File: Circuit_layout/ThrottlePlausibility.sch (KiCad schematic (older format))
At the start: 56 parts, among them Q2 MMBF170, SW1 TS5A3159-Q1, U1 LM7332, U17 MCP6004, U3 MCP6004, U4 MCP6004, U5 LM7332, U6 LM339, U8 74ACT11030

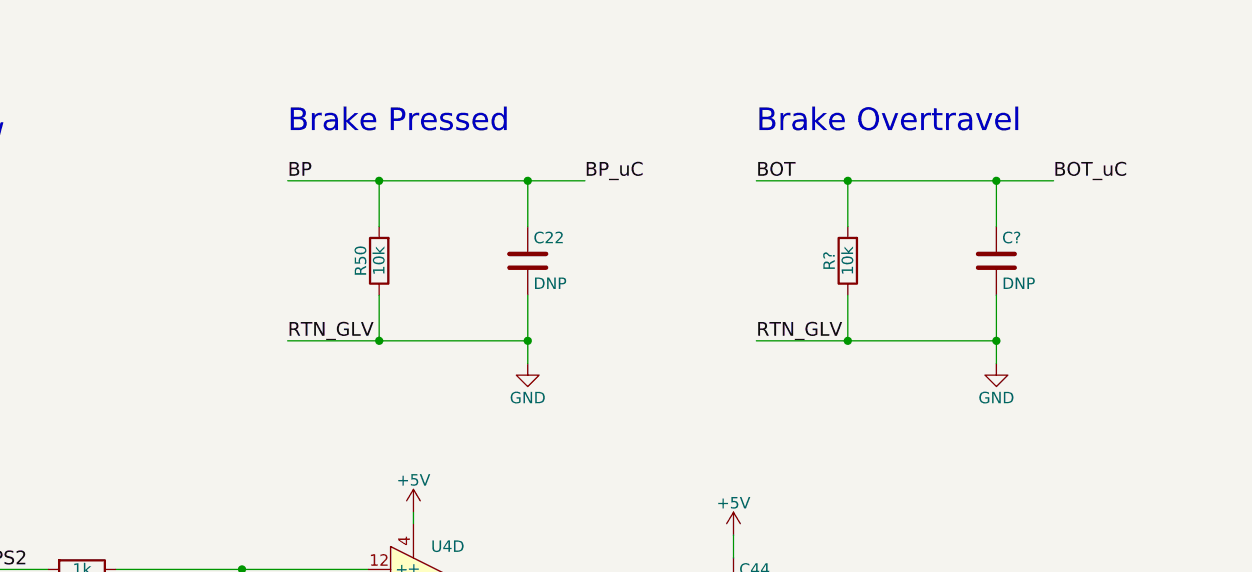
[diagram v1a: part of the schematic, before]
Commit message: added optoiso for brake overtravel
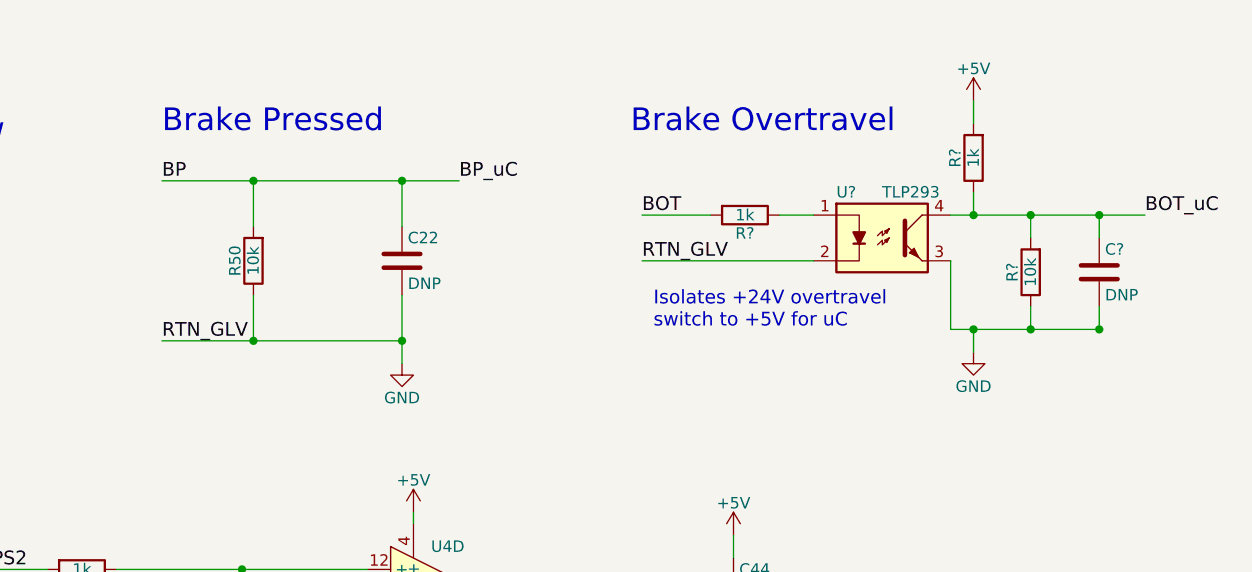
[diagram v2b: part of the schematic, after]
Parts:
- removed C?: DNP, Capacitors_SMD:C_0805_HandSoldering, symbol C
- removed R?: 10k, Resistors_SMD:R_0805_HandSoldering, symbol R
- added C?: DNP, Capacitors_SMD:C_0805_HandSoldering, symbol C
- added R? (x2): 1k, Resistors_SMD:R_0805_HandSoldering, symbol R
- added R?: 10k, Resistors_SMD:R_0805_HandSoldering, symbol R
- added U?: TLP293, Housings_SSOP:SOP-4_4.4x2.8mm_Pitch1.27mm, symbol TLP291
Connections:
- wire segments 182 -> 189
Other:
- note added: "Isolates +24V overtravel \nswitch to +5V for uC"
- moved on the sheet: C22, R50
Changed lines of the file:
@@
 BP_uC
 Wire Wire Line
-	12350 2150 12350 1950
-Text Label 11950 1450 0    60   ~ 0
+	11800 2150 11800 1950
+Text Label 11400 1450 0    60   ~ 0
 BP
 Wire Wire Line
-	12350 1450 12350 1650
-Text Label 11950 2150 0    60   ~ 0
+	11800 1450 11800 1650
+Text Label 11400 2150 0    60   ~ 0
 RTN_GLV
 Wire Wire Line
-	11950 1450 13250 1450
-Wire Wire Line
-	11950 2150 13000 2150
-Connection ~ 12350 1450
-Connection ~ 12350 2150
+	11400 1450 12700 1450
+Wire Wire Line
+	11400 2150 12450 2150
+Connection ~ 11800 1450
+Connection ~ 11800 2150
 $Comp
 L C C22
 U 1 1 58AE29E7
-P 13000 1800
-F 0 "C22" H 13025 1900 50  0000 L CNN
-F 1 "DNP" H 13025 1700 50  0000 L CNN
-F 2 "Capacitors_SMD:C_0805_HandSoldering" H 13038 1650 50  0001 C CNN
-F 3 "" H 13000 1800 50  0000 C CNN
-	1    13000 1800
-	1    0    0    -1
-$EndComp
-Wire Wire Line
-	13000 1950 13000 2250
-Connection ~ 13000 2150
-Wire Wire Line
-	13000 1650 13000 1450
-Connection ~ 13000 1450
-Text Label 13250 1450 0    60   ~ 0
+P 12450 1800
+F 0 "C22" H 12475 1900 50  0000 L CNN
+F 1 "DNP" H 12475 1700 50  0000 L CNN
+F 2 "Capacitors_SMD:C_0805_HandSoldering" H 12488 1650 50  0001 C CNN
+F 3 "" H 12450 1800 50  0000 C CNN
+	1    12450 1800
+	1    0    0    -1
+$EndComp
+Wire Wire Line
+	12450 1950 12450 2250
+Connection ~ 12450 2150
+Wire Wire Line
+	12450 1650 12450 1450
+Connection ~ 12450 1450
+Text Label 12700 1450 0    60   ~ 0
 BP_uC
 Wire Wire Line
@@
 Text Label 3600 1100 0    60   ~ 0
 RTN_GLV
-Text Notes 11950 1250 0    99   ~ 0
+Text Notes 11400 1250 0    99   ~ 0
 Brake Pressed
 $Comp
 L GND #PWR087
 U 1 1 58B4B2A9
-P 13000 2250
-F 0 "#PWR087" H 13000 2000 50  0001 C CNN
-F 1 "GND" H 13000 2100 50  0000 C CNN
-F 2 "" H 13000 2250 50  0000 C CNN
-F 3 "" H 13000 2250 50  0000 C CNN
-	1    13000 2250
+P 12450 2250
+F 0 "#PWR087" H 12450 2000 50  0001 C CNN
+F 1 "GND" H 12450 2100 50  0000 C CNN
+F 2 "" H 12450 2250 50  0000 C CNN
+F 3 "" H 12450 2250 50  0000 C CNN
+	1    12450 2250
 	1    0    0    -1
 $EndComp
@@
 L R R50
 U 1 1 58B79345
-P 12350 1800
-F 0 "R50" V 12430 1800 50  0000 C CNN
-F 1 "10k" V 12350 1800 50  0000 C CNN
-F 2 "Resistors_SMD:R_0805_HandSoldering" V 12280 1800 50  0001 C CNN
-F 3 "" H 12350 1800 50  0000 C CNN
-F 4 "P10.0KCCT-ND" V 12350 1800 60  0001 C CNN "DigiKey P/N"
-F 5 "http://www.digikey.com/product-detail/en/panasonic-electronic-components/ERJ-6ENF1002V/P10.0KCCT-ND/119248" V 12350 1800 60  0001 C CNN "URL"
-F 6 "ERJ-6ENF1002V" V 12350 1800 60  0001 C CNN "Man P/N"
-	1    12350 1800
+P 11800 1800
+F 0 "R50" V 11880 1800 50  0000 C CNN
+F 1 "10k" V 11800 1800 50  0000 C CNN
+F 2 "Resistors_SMD:R_0805_HandSoldering" V 11730 1800 50  0001 C CNN
+F 3 "" H 11800 1800 50  0000 C CNN
+F 4 "P10.0KCCT-ND" V 11800 1800 60  0001 C CNN "DigiKey P/N"
+F 5 "http://www.digikey.com/product-detail/en/panasonic-electronic-components/ERJ-6ENF1002V/P10.0KCCT-ND/119248" V 11800 1800 60  0001 C CNN "URL"
+F 6 "ERJ-6ENF1002V" V 11800 1800 60  0001 C CNN "Man P/N"
+	1    11800 1800
 	-1   0    0    1
 $EndComp
@@
 $EndComp
 Connection ~ 3100 6000
-Wire Wire Line
-	14400 2150 14400 1950
-Text Label 14000 1450 0    60   ~ 0
-BOT
-Wire Wire Line
-	14400 1450 14400 1650
-Text Label 14000 2150 0    60   ~ 0
+Text Label 13500 1800 0    60   ~ 0
 RTN_GLV
-Wire Wire Line
-	14000 1450 15300 1450
-Wire Wire Line
-	14000 2150 15050 2150
-Connection ~ 14400 1450
-Connection ~ 14400 2150
-$Comp
-L C C?
-U 1 1 58BE3051
-P 15050 1800
-F 0 "C?" H 15075 1900 50  0000 L CNN
-F 1 "DNP" H 15075 1700 50  0000 L CNN
-F 2 "Capacitors_SMD:C_0805_HandSoldering" H 15088 1650 50  0001 C CNN
-F 3 "" H 15050 1800 50  0000 C CNN
-	1    15050 1800
-	1    0    0    -1
-$EndComp
-Wire Wire Line
-	15050 1950 15050 2250
-Connection ~ 15050 2150
-Wire Wire Line
-	15050 1650 15050 1450
-Connection ~ 15050 1450
-Text Label 15300 1450 0    60   ~ 0
-BOT_uC
-Text Notes 14000 1250 0    99   ~ 0
+Text Notes 13450 1250 0    99   ~ 0
 Brake Overtravel
-$Comp
-L GND #PWR?
-U 1 1 58BE305D
-P 15050 2250
-F 0 "#PWR?" H 15050 2000 50  0001 C CNN
-F 1 "GND" H 15050 2100 50  0000 C CNN
-F 2 "" H 15050 2250 50  0000 C CNN
-F 3 "" H 15050 2250 50  0000 C CNN
-	1    15050 2250
-	1    0    0    -1
-$EndComp
-$Comp
-L R R?
-U 1 1 58BE3067
-P 14400 1800
-F 0 "R?" V 14480 1800 50  0000 C CNN
-F 1 "10k" V 14400 1800 50  0000 C CNN
-F 2 "Resistors_SMD:R_0805_HandSoldering" V 14330 1800 50  0001 C CNN
-F 3 "" H 14400 1800 50  0000 C CNN
-F 4 "P10.0KCCT-ND" V 14400 1800 60  0001 C CNN "DigiKey P/N"
-F 5 "http://www.digikey.com/product-detail/en/panasonic-electronic-components/ERJ-6ENF1002V/P10.0KCCT-ND/119248" V 14400 1800 60  0001 C CNN "URL"
-F 6 "ERJ-6ENF1002V" V 14400 1800 60  0001 C CNN "Man P/N"
-	1    14400 1800
-	-1   0    0    1
-$EndComp
 Wire Wire Line
 	3250 1500 3450 1500
@@
 Text Label 3400 1950 0    60   ~ 0
 BOT_uC
+$Comp
+L TLP291 U?
+U 1 1 58BF52E8
+P 14550 1700
+F 0 "U?" H 14350 1900 50  0000 L CNN
+F 1 "TLP293" H 14550 1900 50  0000 L CNN
+F 2 "Housings_SSOP:SOP-4_4.4x2.8mm_Pitch1.27mm" H 14350 1500 50  0001 L CIN
+F 3 "" H 14550 1700 50  0000 L CNN
+F 4 "TLP293(GB-TPLECT-ND" H 14550 1700 60  0001 C CNN "DigiKey P/N"
+F 5 "http://www.digikey.com/product-detail/en/toshiba-semiconductor-and-storage/TLP293(GB-TPL,E/TLP293(GB-TPLECT-ND/4562965" H 14550 1700 60  0001 C CNN "URL"
+F 6 "TLP293(GB-TPLE" H 14550 1700 60  0001 C CNN "Man P/N"
+F 7 "http://www.digikey.com/product-detail/en/toshiba-semiconductor-and-storage/TLP291(GB-TP,SE/TLP291(GB-TPSECT-ND/4562949" H 14550 1700 60  0001 C CNN "TLP291"
+	1    14550 1700
+	1    0    0    -1
+$EndComp
+$Comp
+L R R?
+U 1 1 58BF52F2
+P 13950 1600
+F 0 "R?" V 14030 1600 50  0000 C CNN
+F 1 "1k" V 13950 1600 50  0000 C CNN
+F 2 "Resistors_SMD:R_0805_HandSoldering" V 13880 1600 50  0001 C CNN
+F 3 "" H 13950 1600 50  0000 C CNN
+F 4 "P1.00KCCT-ND" V 13950 1600 60  0001 C CNN "DigiKey P/N"
+F 5 "http://www.digikey.com/product-detail/en/panasonic-electronic-components/ERJ-6ENF1001V/P1.00KCCT-ND/118957" V 13950 1600 60  0001 C CNN "URL"
+F 6 "ERJ-6ENF1001V" V 13950 1600 60  0001 C CNN "Man P/N"
+	1    13950 1600
+	0    1    1    0
+$EndComp
+$Comp
+L R R?
+U 1 1 58BF52FC
+P 14950 1350
+F 0 "R?" V 15030 1350 50  0000 C CNN
+F 1 "1k" V 14950 1350 50  0000 C CNN
+F 2 "Resistors_SMD:R_0805_HandSoldering" V 14880 1350 50  0001 C CNN
+F 3 "" H 14950 1350 50  0000 C CNN
+F 4 "P1.00KCCT-ND" V 14950 1350 60  0001 C CNN "DigiKey P/N"
+F 5 "http://www.digikey.com/product-detail/en/panasonic-electronic-components/ERJ-6ENF1001V/P1.00KCCT-ND/118957" V 14950 1350 60  0001 C CNN "URL"
+F 6 "ERJ-6ENF1001V" V 14950 1350 60  0001 C CNN "Man P/N"
+	1    14950 1350
+	-1   0    0    1
+$EndComp
+$Comp
+L GND #PWR?
+U 1 1 58BF5303
+P 14950 2200
+F 0 "#PWR?" H 14950 1950 50  0001 C CNN
+F 1 "GND" H 14950 2050 50  0000 C CNN
+F 2 "" H 14950 2200 50  0000 C CNN
+F 3 "" H 14950 2200 50  0000 C CNN
+	1    14950 2200
+	1    0    0    -1
+$EndComp
+$Comp
+L +5V #PWR?
+U 1 1 58BF60CD
+P 14950 1100
+F 0 "#PWR?" H 14950 950 50  0001 C CNN
+F 1 "+5V" H 14950 1240 50  0000 C CNN
+F 2 "" H 14950 1100 50  0000 C CNN
+F 3 "" H 14950 1100 50  0000 C CNN
+	1    14950 1100
+	1    0    0    -1
+$EndComp
+$Comp
+L R R?
+U 1 1 58BF69A9
+P 15200 1850
+F 0 "R?" V 15280 1850 50  0000 C CNN
+F 1 "10k" V 15200 1850 50  0000 C CNN
+F 2 "Resistors_SMD:R_0805_HandSoldering" V 15130 1850 50  0001 C CNN
+F 3 "" H 15200 1850 50  0000 C CNN
+F 4 "P10.0KCCT-ND" V 15200 1850 60  0001 C CNN "DigiKey P/N"
+F 5 "http://www.digikey.com/product-detail/en/panasonic-electronic-components/ERJ-6ENF1002V/P10.0KCCT-ND/119248" V 15200 1850 60  0001 C CNN "URL"
+F 6 "ERJ-6ENF1002V" V 15200 1850 60  0001 C CNN "Man P/N"
+	1    15200 1850
+	-1   0    0    1
+$EndComp
+$Comp
+L C C?
+U 1 1 58BF6C5C
+P 15500 1850
+F 0 "C?" H 15525 1950 50  0000 L CNN
+F 1 "DNP" H 15525 1750 50  0000 L CNN
+F 2 "Capacitors_SMD:C_0805_HandSoldering" H 15538 1700 50  0001 C CNN
+F 3 "" H 15500 1850 50  0000 C CNN
+	1    15500 1850
+	1    0    0    -1
+$EndComp
+Wire Wire Line
+	15500 1600 15500 1700
+Connection ~ 15500 1600
+Text Label 15700 1600 0    60   ~ 0
+BOT_uC
+Wire Wire Line
+	14850 1800 14850 2100
+Wire Wire Line
+	15500 2100 15500 2000
+Connection ~ 15500 2100
+Text Label 13500 1600 0    60   ~ 0
+BOT
+Wire Wire Line
+	13500 1600 13800 1600
+Wire Wire Line
+	14100 1600 14250 1600
+Wire Wire Line
+	13500 1800 14250 1800
+Wire Wire Line
+	14850 1600 15700 1600
+Wire Wire Line
+	14950 1500 14950 1600
+Connection ~ 14950 1600
+Wire Wire Line
+	15200 1700 15200 1600
+Connection ~ 15200 1600
+Wire Wire Line
+	14850 2100 15500 2100
+Wire Wire Line
+	15200 2100 15200 2000
+Connection ~ 15200 2100
+Wire Wire Line
+	14950 2200 14950 2100
+Connection ~ 14950 2100
+Wire Wire Line
+	14950 1100 14950 1200
+Text Notes 13550 2100 0    60   ~ 0
+Isolates +24V overtravel \nswitch to +5V for uC
 $EndSCHEMATC

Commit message: need to make further changes after review w/ prof
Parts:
- removed C20, C24: 15p, Capacitors_SMD:C_0805_HandSoldering, symbol C
- removed R?: 1k, Resistors_SMD:R_0805_HandSoldering, symbol R
- removed SW1: TS5A3159-Q1, TO_SOT_Packages_SMD:SOT-23-6_Handsoldering, symbol TS5A3159-Q1
- added JP?: JUMPER3, symbol JUMPER3
- added R?: 10k, Resistors_SMD:R_0805_HandSoldering, symbol R
- added U? (x2): MCP6004, Housings_SOIC:SOIC-14_3.9x8.7mm_Pitch1.27mm, symbol MCP6004
- renumbered U17 to U3
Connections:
- wire segments 189 -> 188
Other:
- note added: "Add brake input"
- note added: "Change to jumper"
- note added: "Fix BOT"
- note added: "Inv. signal\nCurr. Xfer. Ratio=200% \n(w/in rng)"
- note removed: "Isolates +24V overtravel \nswitch to +5V for uC"
- moved on the sheet: R25

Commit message: changes before presentation
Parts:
- removed C13, C39: 0.1u, Capacitors_SMD:C_0805_HandSoldering, symbol C
- removed C?: DNP, Capacitors_SMD:C_0805_HandSoldering, symbol C
- removed R21, R?: 1k, Resistors_SMD:R_0805_HandSoldering, symbol R
- removed R? (x2): 10k, Resistors_SMD:R_0805_HandSoldering, symbol R
- removed U1, U5: LM7332, Housings_SOIC:SOIC-8_3.9x4.9mm_Pitch1.27mm, symbol LM7332
- removed U6: LM339, Housings_SOIC:SOIC-14_3.9x8.7mm_Pitch1.27mm, symbol LM339
- removed U?: BAJ0CC0FP-E2, symbol BAJ0CC0FP-E2
- removed U? (x2): MCP6004, Housings_SOIC:SOIC-14_3.9x8.7mm_Pitch1.27mm, symbol MCP6004
- added C20, C23: 0.1u, Capacitors_SMD:C_0805_HandSoldering, symbol C
- added R39, R42: 10k, Resistors_SMD:R_0805_HandSoldering, symbol R
- added R51, R52: 250k, Resistors_SMD:R_0805_HandSoldering, symbol R
- added SW2: TS5A3159, symbol SWITCH_INV
- added U18, U6: TS912, Housings_SOIC:SOIC-8_3.9x4.9mm_Pitch1.27mm, symbol TS912
- added U22: TS372, Housings_SOIC:SOIC-8_3.9x4.9mm_Pitch1.27mm, symbol TS372
- added U23: TLP293, Housings_SSOP:SOP-4_4.4x2.8mm_Pitch1.27mm, symbol TLP291
- added U5: LM7810CT, TO-220, symbol LM7810CT
- C22: value DNP -> 0.1u; Digikey P/N (none) -> 399-1168-1-ND; Man P/N (none) -> C0805C104K3RACTU; URL (none) -> http://www.digikey.com/product-detail/en/kemet/C0805C104K3R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
- R22, R23, R28, R29, R31: value 1k -> 10k; DigiKey P/N P1.00KCCT-ND -> P10.0KCCT-ND; Man P/N ERJ-6ENF1001V -> ERJ-6ENF1002V; URL http://www.digikey.com/product-detail/en/panasonic-electronic-components/ERJ-6ENF1001V/P1.00KCCT-ND/118957 -> http://www.digikey.com/product-detail/en/panasonic-electronic-components/ERJ-6ENF1002V/P10.0KCCT-ND/119248
- R24, R30: value 1k -> 100k; Cost (none) -> 0.10; Description (none) -> RES SMD 100K OHM 1% 1/8W 0805; DigiKey P/N P1.00KCCT-ND -> P100KCCT-ND; Man P/N ERJ-6ENF1001V -> ERJ-6ENF1003V; URL http://www.digikey.com/product-detail/en/panasonic-electronic-components/ERJ-6ENF1001V/P1.00KCCT-ND/118957 -> http://www.digikey.com/product-detail/en/panasonic-electronic-components/ERJ-6ENF1003V/P100KCCT-ND/119551
- gave numbers to parts that had none: 2
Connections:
- net labels added: APPS1_b, APPS2_b
- net labels removed: +12V
- wire segments 188 -> 212
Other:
- note added: "APPS 5V Offset Bias"
- note added: "Inv. signal\nCurr. Transfer. Ratio=100% \n"
- note added: "Used for 10V \nrail-to-rail ability"
- note removed: "0.3V LDO Regul."
- note removed: "Add brake input"
- note removed: "Change to jumper"
- note removed: "Fix BOT"
- note removed: "Inv. signal\nCurr. Xfer. Ratio=200% \n(w/in rng)"
- note removed: "Resistors Set for maximum\nof 90% travel ( > will trigger fault)"
- note removed: "Used for 10V \nrail-to-rail ability\n\nCheck footprint"
- moved on the sheet: C12, C17, C26, C45, R25, R26, R45, R47, R49, R53, U4A

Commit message: pics of schematic
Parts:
- SW2: symbol SWITCH_INV -> SWITCH_INV-RESCUE-Circuit_layout
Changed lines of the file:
@@
 LIBS:xilinx
 LIBS:Zilog
-LIBS:pacman-main-cache
 LIBS:bss84
 LIBS:+10v
@@
 $EndComp
 $Comp
-L SWITCH_INV SW2
+L SWITCH_INV-RESCUE-Circuit_layout SW2
 U 1 1 58C5A230
 P 14450 4800
+AR Path="/58C5A230" Ref="SW2"  Part="1"
+AR Path="/58A289D2/58C5A230" Ref="SW2"  Part="1"
 F 0 "SW2" H 14250 4950 50  0000 C CNN
 F 1 "TS5A3159" H 14150 4650 50  0000 C CNN

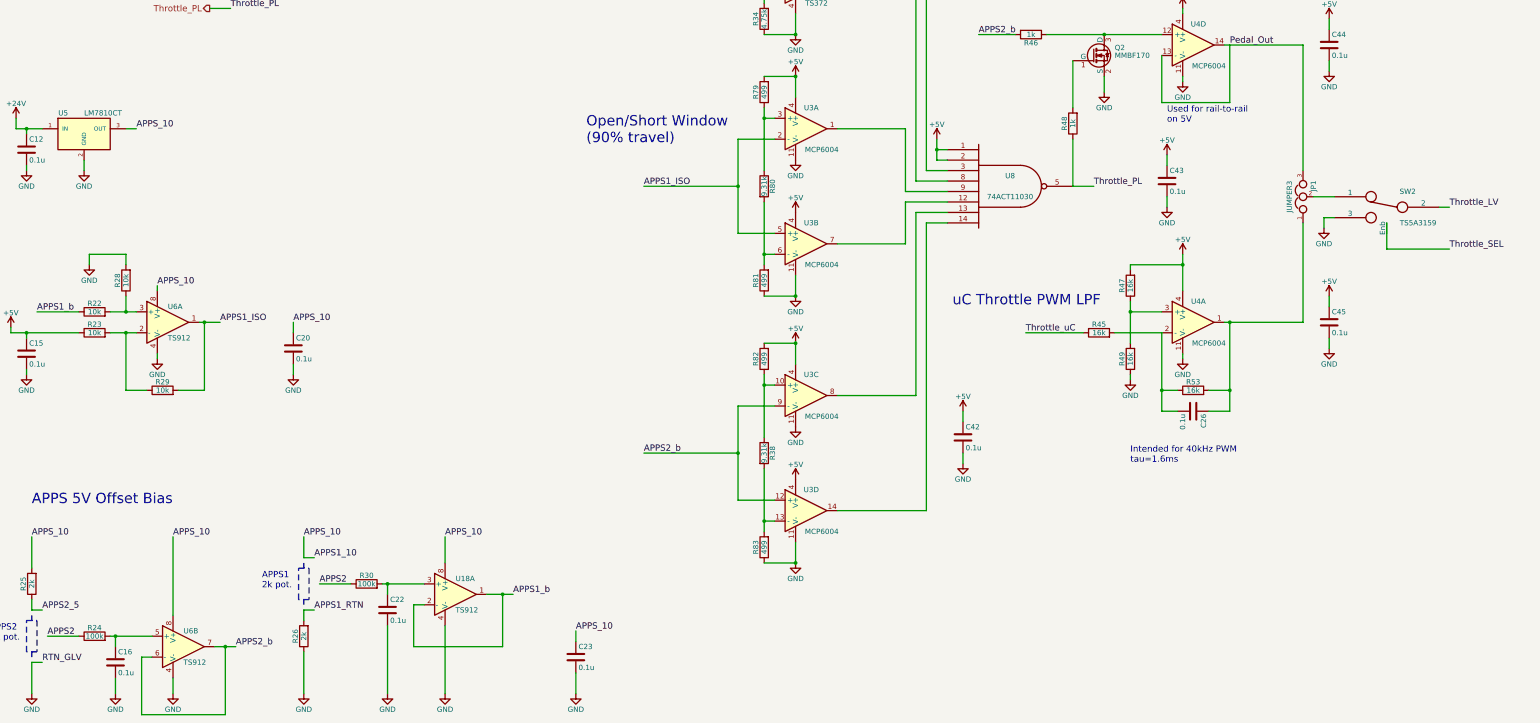
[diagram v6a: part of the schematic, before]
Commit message: added test pts
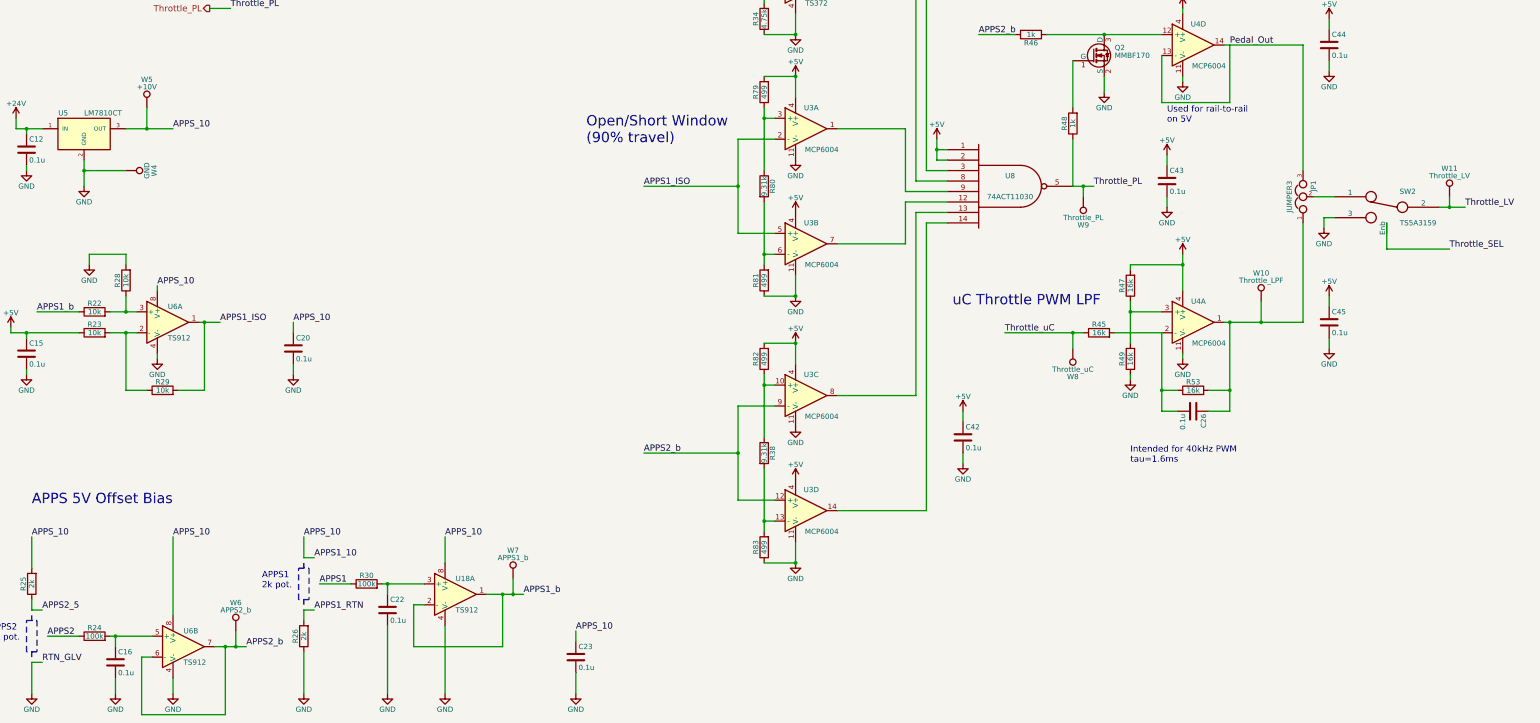
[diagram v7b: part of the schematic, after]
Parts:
- added W10: Throttle_LPF, symbol TEST_1P
- added W11: Throttle_LV, symbol TEST_1P
- added W4: GND, symbol TEST_1P
- added W5: +10V, symbol TEST_1P
- added W6: APPS2_b, symbol TEST_1P
- added W7: APPS1_b, symbol TEST_1P
- added W8: Throttle_uC, symbol TEST_1P
- added W9: Throttle_PL, symbol TEST_1P
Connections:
- net APPS1: now also R30.1
- net APPS1_10: now also W5.1
- net APPS1_b: now also W7.1
- net APPS2: no longer R30.1
- net APPS2_b: now also W6.1
- net GND: now also W4.1
- net Throttle_LV: now also W11.1
- net Throttle_PL: now also W9.1
- net Throttle_uC: now also W8.1
- net at C26.1, JP1.1, R53.2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: now also W10.1
